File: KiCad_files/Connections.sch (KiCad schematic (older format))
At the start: 6 parts

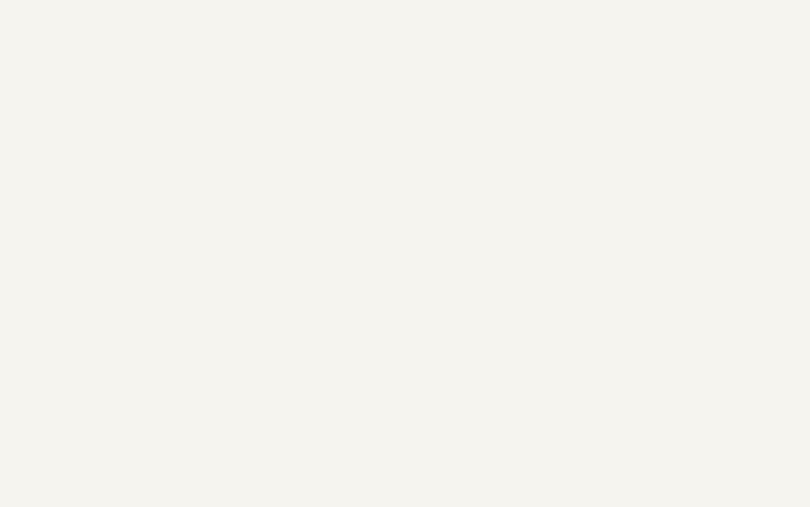
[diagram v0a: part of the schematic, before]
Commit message: Added VGA
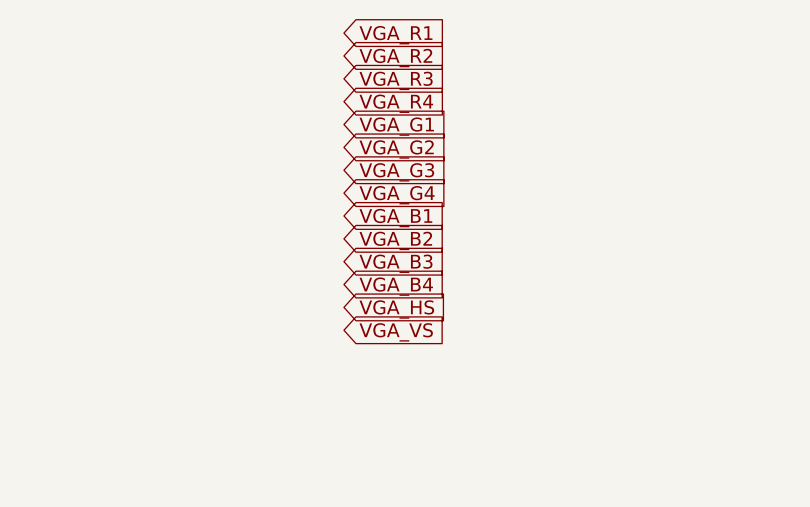
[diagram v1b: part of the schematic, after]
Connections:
- net labels added: VGA_B1, VGA_B2, VGA_B3, VGA_B4, VGA_G1, VGA_G2, VGA_G3, VGA_G4, VGA_HS, VGA_R1, VGA_R2, VGA_R3, VGA_R4, VGA_VS
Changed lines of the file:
@@
 Text GLabel 3150 3100 2    60   Input ~ 0
 SYSCLK_P
+Text GLabel 6300 1400 2    60   Input ~ 0
+VGA_R1
+Text GLabel 6300 1500 2    60   Input ~ 0
+VGA_R2
+Text GLabel 6300 1600 2    60   Input ~ 0
+VGA_R3
+Text GLabel 6300 1700 2    60   Input ~ 0
+VGA_R4
+Text GLabel 6300 1800 2    60   Input ~ 0
+VGA_G1
+Text GLabel 6300 1900 2    60   Input ~ 0
+VGA_G2
+Text GLabel 6300 2000 2    60   Input ~ 0
+VGA_G3
+Text GLabel 6300 2100 2    60   Input ~ 0
+VGA_G4
+Text GLabel 6300 2200 2    60   Input ~ 0
+VGA_B1
+Text GLabel 6300 2300 2    60   Input ~ 0
+VGA_B2
+Text GLabel 6300 2400 2    60   Input ~ 0
+VGA_B3
+Text GLabel 6300 2500 2    60   Input ~ 0
+VGA_B4
+Text GLabel 6300 2600 2    60   Input ~ 0
+VGA_HS
+Text GLabel 6300 2700 2    60   Input ~ 0
+VGA_VS
 $EndSCHEMATC

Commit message: DDR RAM 32 bits instead of 64bits
Don't have enough pins :(
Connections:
- net labels added: DDR4_A0, DDR4_A1, DDR4_A10, DDR4_A11, DDR4_A12, DDR4_A13, DDR4_A14_WE_B, DDR4_A15_CAS_B, DDR4_A16_RAS_B, DDR4_A2, DDR4_A3, DDR4_A4, DDR4_A5, DDR4_A6, DDR4_A7, DDR4_A8, DDR4_A9, DDR4_ACT_N, DDR4_ALERT_N, DDR4_BA0, DDR4_BA1, DDR4_BG0, DDR4_CKE, DDR4_CK_C, DDR4_CK_T, DDR4_CS_N, DDR4_DM0, DDR4_DM1, DDR4_DM2, DDR4_DM3, DDR4_DQ0, DDR4_DQ1, DDR4_DQ10, DDR4_DQ11, DDR4_DQ12, DDR4_DQ13, DDR4_DQ14, DDR4_DQ15, DDR4_DQ16, DDR4_DQ17, DDR4_DQ18, DDR4_DQ19, DDR4_DQ2, DDR4_DQ20, DDR4_DQ21, DDR4_DQ22, DDR4_DQ23, DDR4_DQ24, DDR4_DQ25, DDR4_DQ26, DDR4_DQ27, DDR4_DQ28, DDR4_DQ29, DDR4_DQ3, DDR4_DQ30, DDR4_DQ31, DDR4_DQ4, DDR4_DQ5, DDR4_DQ6, DDR4_DQ7, DDR4_DQ8, DDR4_DQ9, DDR4_DQS0_C, DDR4_DQS0_T, DDR4_DQS1_C, DDR4_DQS1_T, DDR4_DQS2_C, DDR4_DQS2_T, DDR4_DQS3_C, DDR4_DQS3_T, DDR4_ODT, DDR4_PAR, DDR4_RESET_N, DDR4_TEN
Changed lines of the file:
@@
 $Descr A4 11693 8268
 encoding utf-8
-Sheet 7 13
+Sheet 7 10
 Title "Reconfigurable Application-Specific Accelerator Card"
 Date "2018-11-27"
@@
 Text GLabel 6300 2700 2    60   Input ~ 0
 VGA_VS
+Text GLabel 6300 2800 2    60   Input ~ 0
+DDR4_A0
+Text GLabel 6300 2900 2    60   Input ~ 0
+DDR4_A1
+Text GLabel 6300 3000 2    60   Input ~ 0
+DDR4_A2
+Text GLabel 6300 3100 2    60   Input ~ 0
+DDR4_A3
+Text GLabel 6300 3200 2    60   Input ~ 0
+DDR4_A4
+Text GLabel 6300 3300 2    60   Input ~ 0
+DDR4_A5
+Text GLabel 6300 3400 2    60   Input ~ 0
+DDR4_A6
+Text GLabel 6300 3500 2    60   Input ~ 0
+DDR4_A7
+Text GLabel 6300 3600 2    60   Input ~ 0
+DDR4_A8
+Text GLabel 6300 3700 2    60   Input ~ 0
+DDR4_A9
+Text GLabel 6300 3800 2    60   Input ~ 0
+DDR4_A10
+Text GLabel 6300 3900 2    60   Input ~ 0
+DDR4_A11
+Text GLabel 6300 4000 2    60   Input ~ 0
+DDR4_A12
+Text GLabel 6300 4100 2    60   Input ~ 0
+DDR4_A13
+Text GLabel 6300 4200 2    60   Input ~ 0
+DDR4_A14_WE_B
+Text GLabel 6300 4300 2    60   Input ~ 0
+DDR4_A15_CAS_B
+Text GLabel 6300 4400 2    60   Input ~ 0
+DDR4_A16_RAS_B
+Text GLabel 6300 4500 2    60   Input ~ 0
+DDR4_BA0
+Text GLabel 6300 4600 2    60   Input ~ 0
+DDR4_BA1
+Text GLabel 6300 4700 2    60   Input ~ 0
+DDR4_BG0
+Text GLabel 6300 4800 2    60   Input ~ 0
+DDR4_CK_T
+Text GLabel 6300 4900 2    60   Input ~ 0
+DDR4_CK_C
+Text GLabel 6300 5000 2    60   Input ~ 0
+DDR4_CKE
+Text GLabel 6300 5100 2    60   Input ~ 0
+DDR4_ACT_N
+Text GLabel 6300 5200 2    60   Input ~ 0
+DDR4_TEN
+Text GLabel 6300 5300 2    60   Input ~ 0
+DDR4_ALERT_N
+Text GLabel 6300 5400 2    60   Input ~ 0
+DDR4_PAR
+Text GLabel 6300 5500 2    60   Input ~ 0
+DDR4_RESET_N
+Text GLabel 6300 5600 2    60   Input ~ 0
+DDR4_ODT
+Text GLabel 6300 5700 2    60   Input ~ 0
+DDR4_CS_N
+Text GLabel 9000 950  2    60   Input ~ 0
+DDR4_DQ0
+Text GLabel 9000 1050 2    60   Input ~ 0
+DDR4_DQ1
+Text GLabel 9000 1150 2    60   Input ~ 0
+DDR4_DQ2
+Text GLabel 9000 1250 2    60   Input ~ 0
+DDR4_DQ3
+Text GLabel 9000 1350 2    60   Input ~ 0
+DDR4_DQ4
+Text GLabel 9000 1450 2    60   Input ~ 0
+DDR4_DQ5
+Text GLabel 9000 1550 2    60   Input ~ 0
+DDR4_DQ6
+Text GLabel 9000 1650 2    60   Input ~ 0
+DDR4_DQ7
+Text GLabel 9000 1750 2    60   Input ~ 0
+DDR4_DQ8
+Text GLabel 9000 1850 2    60   Input ~ 0
+DDR4_DQ9
+Text GLabel 9000 1950 2    60   Input ~ 0
+DDR4_DQ10
+Text GLabel 9000 2050 2    60   Input ~ 0
+DDR4_DQ11
+Text GLabel 9000 2150 2    60   Input ~ 0
+DDR4_DQ12
+Text GLabel 9000 2250 2    60   Input ~ 0
+DDR4_DQ13
+Text GLabel 9000 2350 2    60   Input ~ 0
+DDR4_DQ14
+Text GLabel 9000 2450 2    60   Input ~ 0
+DDR4_DQ15
+Text GLabel 9000 4150 2    60   Input ~ 0
+DDR4_DQS0_T
+Text GLabel 9000 4250 2    60   Input ~ 0
+DDR4_DQS0_C
+Text GLabel 9000 4350 2    60   Input ~ 0
+DDR4_DQS1_T
+Text GLabel 9000 4450 2    60   Input ~ 0
+DDR4_DQS1_C
+Text GLabel 6300 5800 2    60   Input ~ 0
+DDR4_DM0
+Text GLabel 6300 5900 2    60   Input ~ 0
+DDR4_DM1
+Text GLabel 9000 2550 2    60   Input ~ 0
+DDR4_DQ16
+Text GLabel 9000 2650 2    60   Input ~ 0
+DDR4_DQ17
+Text GLabel 9000 2750 2    60   Input ~ 0
+DDR4_DQ18
+Text GLabel 9000 2850 2    60   Input ~ 0
+DDR4_DQ19
+Text GLabel 9000 2950 2    60   Input ~ 0
+DDR4_DQ20
+Text GLabel 9000 3050 2    60   Input ~ 0
+DDR4_DQ21
+Text GLabel 9000 3150 2    60   Input ~ 0
+DDR4_DQ22
+Text GLabel 9000 3250 2    60   Input ~ 0
+DDR4_DQ23
+Text GLabel 9000 3350 2    60   Input ~ 0
+DDR4_DQ24
+Text GLabel 9000 3450 2    60   Input ~ 0
+DDR4_DQ25
+Text GLabel 9000 3550 2    60   Input ~ 0
+DDR4_DQ26
+Text GLabel 9000 3650 2    60   Input ~ 0
+DDR4_DQ27
+Text GLabel 9000 3750 2    60   Input ~ 0
+DDR4_DQ28
+Text GLabel 9000 3850 2    60   Input ~ 0
+DDR4_DQ29
+Text GLabel 9000 3950 2    60   Input ~ 0
+DDR4_DQ30
+Text GLabel 9000 4050 2    60   Input ~ 0
+DDR4_DQ31
+Text GLabel 9000 4550 2    60   Input ~ 0
+DDR4_DQS2_T
+Text GLabel 9000 4650 2    60   Input ~ 0
+DDR4_DQS2_C
+Text GLabel 9000 4750 2    60   Input ~ 0
+DDR4_DQS3_T
+Text GLabel 9000 4850 2    60   Input ~ 0
+DDR4_DQS3_C
+Text GLabel 6300 6000 2    60   Input ~ 0
+DDR4_DM2
+Text GLabel 6300 6100 2    60   Input ~ 0
+DDR4_DM3
 $EndSCHEMATC

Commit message: Cleanup for demo/presentation
Merged Config and Debug sheets.
Added GPIO for remaining pins.
Annotations.
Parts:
- gave numbers to parts that had none: 4
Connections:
- net labels added: GPIO_1, GPIO_10, GPIO_11, GPIO_12, GPIO_13, GPIO_14, GPIO_2, GPIO_3, GPIO_4, GPIO_5, GPIO_6, GPIO_7, GPIO_8, GPIO_9
- net labels removed: HDMI_R_SPDIF, HDMI_SPDIF_OUT_LS

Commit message: Cleanup + Update to KiCad 5.0 + DDR2
Updated to KiCad 5, which re-organized libraries, so corrected them to not need RASAC-rescue.lib.
Also cleaned up some stuff.
DDR4 has been removed and in place will be DDR2.
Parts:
- C86, C87, C88: symbol C -> Device:C
- U1: symbol XC7A35T_CSG325 -> custom:XC7A35T_CSG325
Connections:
- net labels added: DDR2_A0, DDR2_A1, DDR2_A10, DDR2_A11, DDR2_A12, DDR2_A13, DDR2_A14_WE_B, DDR2_A15_CAS_B, DDR2_A16_RAS_B, DDR2_A2, DDR2_A3, DDR2_A4, DDR2_A5, DDR2_A6, DDR2_A7, DDR2_A8, DDR2_A9, DDR2_ACT_N, DDR2_ALERT_N, DDR2_BA0, DDR2_BA1, DDR2_BG0, DDR2_CKE, DDR2_CK_C, DDR2_CK_T, DDR2_CS_N, DDR2_DM0, DDR2_DM1, DDR2_DM2, DDR2_DM3, DDR2_DQ0, DDR2_DQ1, DDR2_DQ10, DDR2_DQ11, DDR2_DQ12, DDR2_DQ13, DDR2_DQ14, DDR2_DQ15, DDR2_DQ16, DDR2_DQ17, DDR2_DQ18, DDR2_DQ19, DDR2_DQ2, DDR2_DQ20, DDR2_DQ21, DDR2_DQ22, DDR2_DQ23, DDR2_DQ24, DDR2_DQ25, DDR2_DQ26, DDR2_DQ27, DDR2_DQ28, DDR2_DQ29, DDR2_DQ3, DDR2_DQ30, DDR2_DQ31, DDR2_DQ4, DDR2_DQ5, DDR2_DQ6, DDR2_DQ7, DDR2_DQ8, DDR2_DQ9, DDR2_DQS0_C, DDR2_DQS0_T, DDR2_DQS1_C, DDR2_DQS1_T, DDR2_DQS2_C, DDR2_DQS2_T, DDR2_DQS3_C, DDR2_DQS3_T, DDR2_ODT, DDR2_PAR, DDR2_RESET_N, DDR2_TEN
- net labels removed: DDR4_A0, DDR4_A1, DDR4_A10, DDR4_A11, DDR4_A12, DDR4_A13, DDR4_A14_WE_B, DDR4_A15_CAS_B, DDR4_A16_RAS_B, DDR4_A2, DDR4_A3, DDR4_A4, DDR4_A5, DDR4_A6, DDR4_A7, DDR4_A8, DDR4_A9, DDR4_ACT_N, DDR4_ALERT_N, DDR4_BA0, DDR4_BA1, DDR4_BG0, DDR4_CKE, DDR4_CK_C, DDR4_CK_T, DDR4_CS_N, DDR4_DM0, DDR4_DM1, DDR4_DM2, DDR4_DM3, DDR4_DQ0, DDR4_DQ1, DDR4_DQ10, DDR4_DQ11, DDR4_DQ12, DDR4_DQ13, DDR4_DQ14, DDR4_DQ15, DDR4_DQ16, DDR4_DQ17, DDR4_DQ18, DDR4_DQ19, DDR4_DQ2, DDR4_DQ20, DDR4_DQ21, DDR4_DQ22, DDR4_DQ23, DDR4_DQ24, DDR4_DQ25, DDR4_DQ26, DDR4_DQ27, DDR4_DQ28, DDR4_DQ29, DDR4_DQ3, DDR4_DQ30, DDR4_DQ31, DDR4_DQ4, DDR4_DQ5, DDR4_DQ6, DDR4_DQ7, DDR4_DQ8, DDR4_DQ9, DDR4_DQS0_C, DDR4_DQS0_T, DDR4_DQS1_C, DDR4_DQS1_T, DDR4_DQS2_C, DDR4_DQS2_T, DDR4_DQS3_C, DDR4_DQS3_T, DDR4_ODT, DDR4_PAR, DDR4_RESET_N, DDR4_TEN
- wire segments 23 -> 40

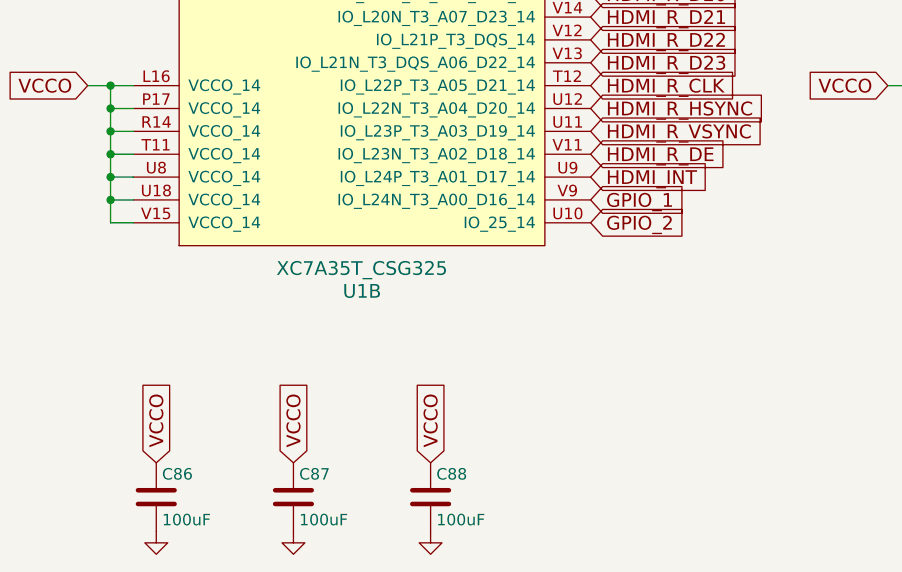
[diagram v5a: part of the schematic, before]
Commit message: Finished HDMI. Added I2C
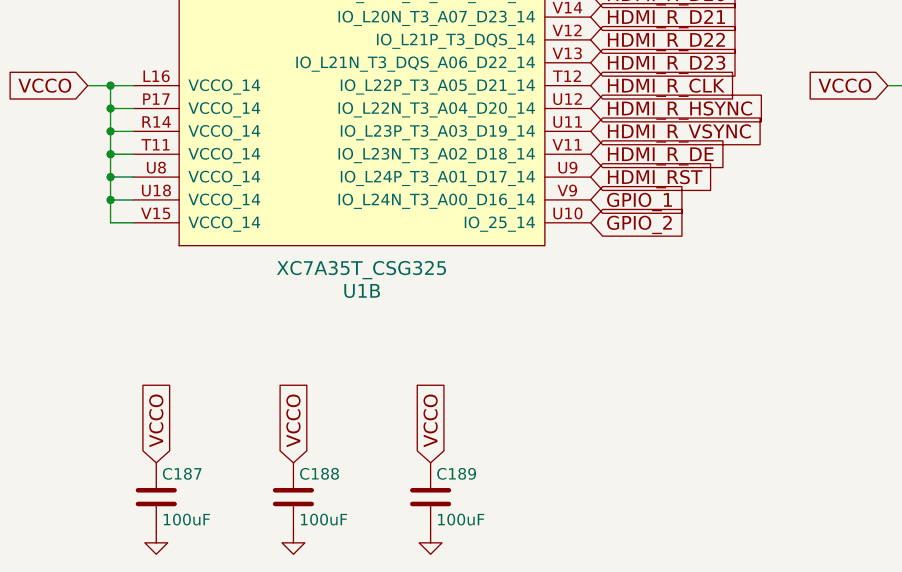
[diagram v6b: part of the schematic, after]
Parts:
- renumbered C86 to C187, C87 to C188, C88 to C189
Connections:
- net HDMI_INT renamed HDMI_RST
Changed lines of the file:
@@
 Connection ~ 1100 5500
 $Comp
-L Device:C C86
+L Device:C C187
 U 1 1 5C113469
 P 1300 7200
-F 0 "C86" H 1325 7300 50  0000 L CNN
+F 0 "C187" H 1325 7300 50  0000 L CNN
 F 1 "100uF" H 1325 7100 50  0000 L CNN
 F 2 "" H 1338 7050 50  0001 C CNN
@@
 VCCO
 $Comp
-L power:GND #PWR091
+L power:GND #PWR097
 U 1 1 5C113471
 P 1300 7350
-F 0 "#PWR091" H 1300 7100 50  0001 C CNN
+F 0 "#PWR097" H 1300 7100 50  0001 C CNN
 F 1 "GND" H 1300 7200 50  0001 C CNN
 F 2 "" H 1300 7350 50  0001 C CNN
@@
 	4500 5400 4600 5400
 $Comp
-L Device:C C87
+L Device:C C188
 U 1 1 5C13C2A0
 P 1900 7200
-F 0 "C87" H 1925 7300 50  0000 L CNN
+F 0 "C188" H 1925 7300 50  0000 L CNN
 F 1 "100uF" H 1925 7100 50  0000 L CNN
 F 2 "" H 1938 7050 50  0001 C CNN
@@
 VCCO
 $Comp
-L power:GND #PWR092
+L power:GND #PWR098
 U 1 1 5C13C2A8
 P 1900 7350
-F 0 "#PWR092" H 1900 7100 50  0001 C CNN
+F 0 "#PWR098" H 1900 7100 50  0001 C CNN
 F 1 "GND" H 1900 7200 50  0001 C CNN
 F 2 "" H 1900 7350 50  0001 C CNN
@@
 	7800 5500 7900 5500
 $Comp
-L Device:C C88
+L Device:C C189
 U 1 1 5C13C2B0
 P 2500 7200
-F 0 "C88" H 2525 7300 50  0000 L CNN
+F 0 "C189" H 2525 7300 50  0000 L CNN
 F 1 "100uF" H 2525 7100 50  0000 L CNN
 F 2 "" H 2538 7050 50  0001 C CNN
@@
 VCCO
 $Comp
-L power:GND #PWR093
+L power:GND #PWR099
 U 1 1 5C13C2B8
 P 2500 7350
-F 0 "#PWR093" H 2500 7100 50  0001 C CNN
+F 0 "#PWR099" H 2500 7100 50  0001 C CNN
 F 1 "GND" H 2500 7200 50  0001 C CNN
 F 2 "" H 2500 7350 50  0001 C CNN
@@
 HDMI_R_CLK
 Text GLabel 3200 5800 2    60   Input ~ 0
-HDMI_INT
+HDMI_RST
 Text GLabel 3200 5500 2    60   Input ~ 0
 HDMI_R_HSYNC
